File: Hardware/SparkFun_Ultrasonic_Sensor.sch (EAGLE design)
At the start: 67 parts, among them J4 Vertical Qwiic Connector, J6 Vertical Qwiic Connector, Q1 600mA/40V, U5 ULTRASONIC_SENSOR_TRANSMITTER, U6 LMV324, U7 STM8L051F3, U8 SP3232EB, U9 ULTRASONIC_SENSOR_RECEIVER

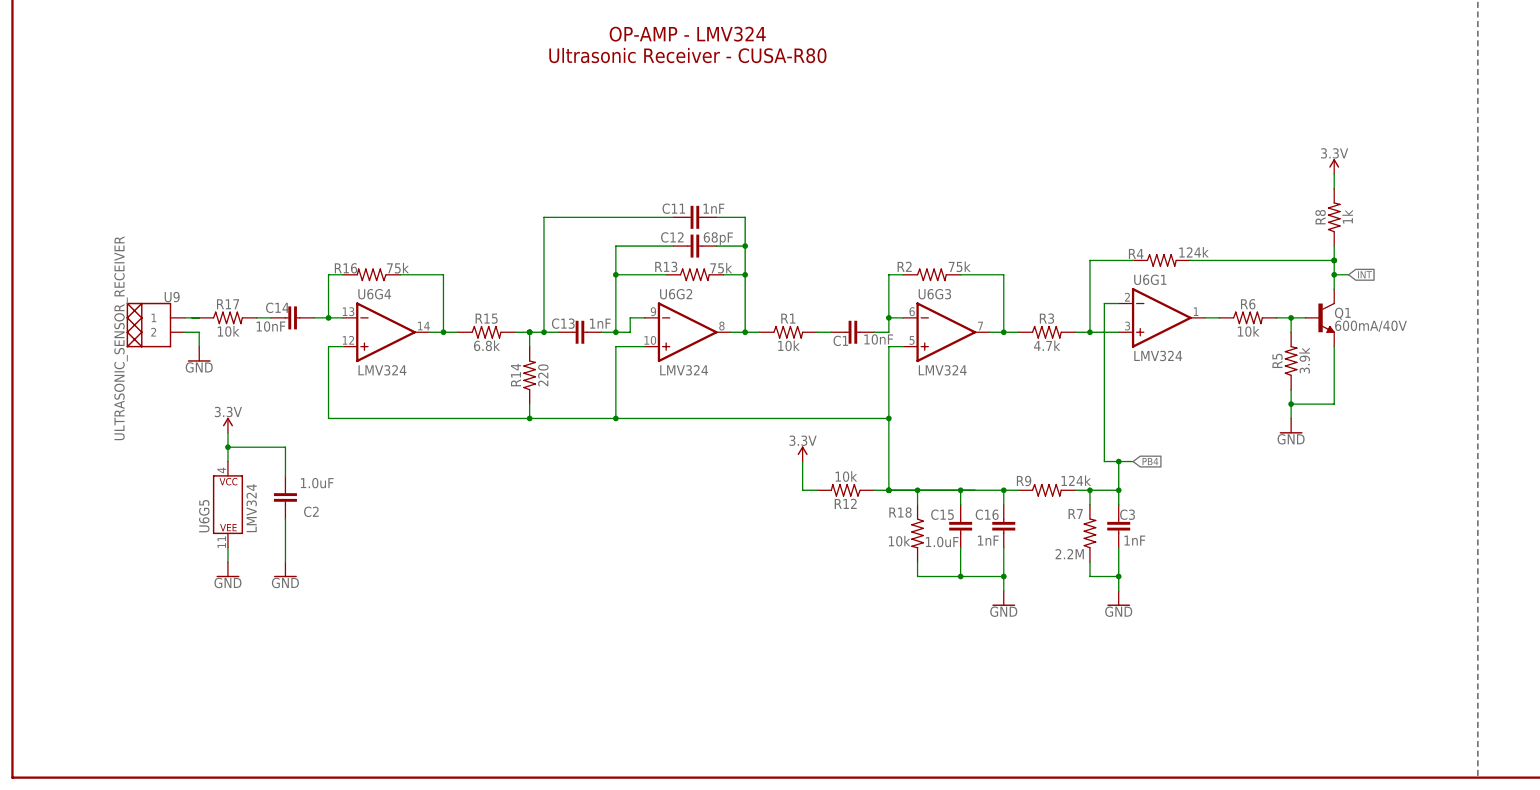
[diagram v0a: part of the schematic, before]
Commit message: Adds some notes on the op-amp stages
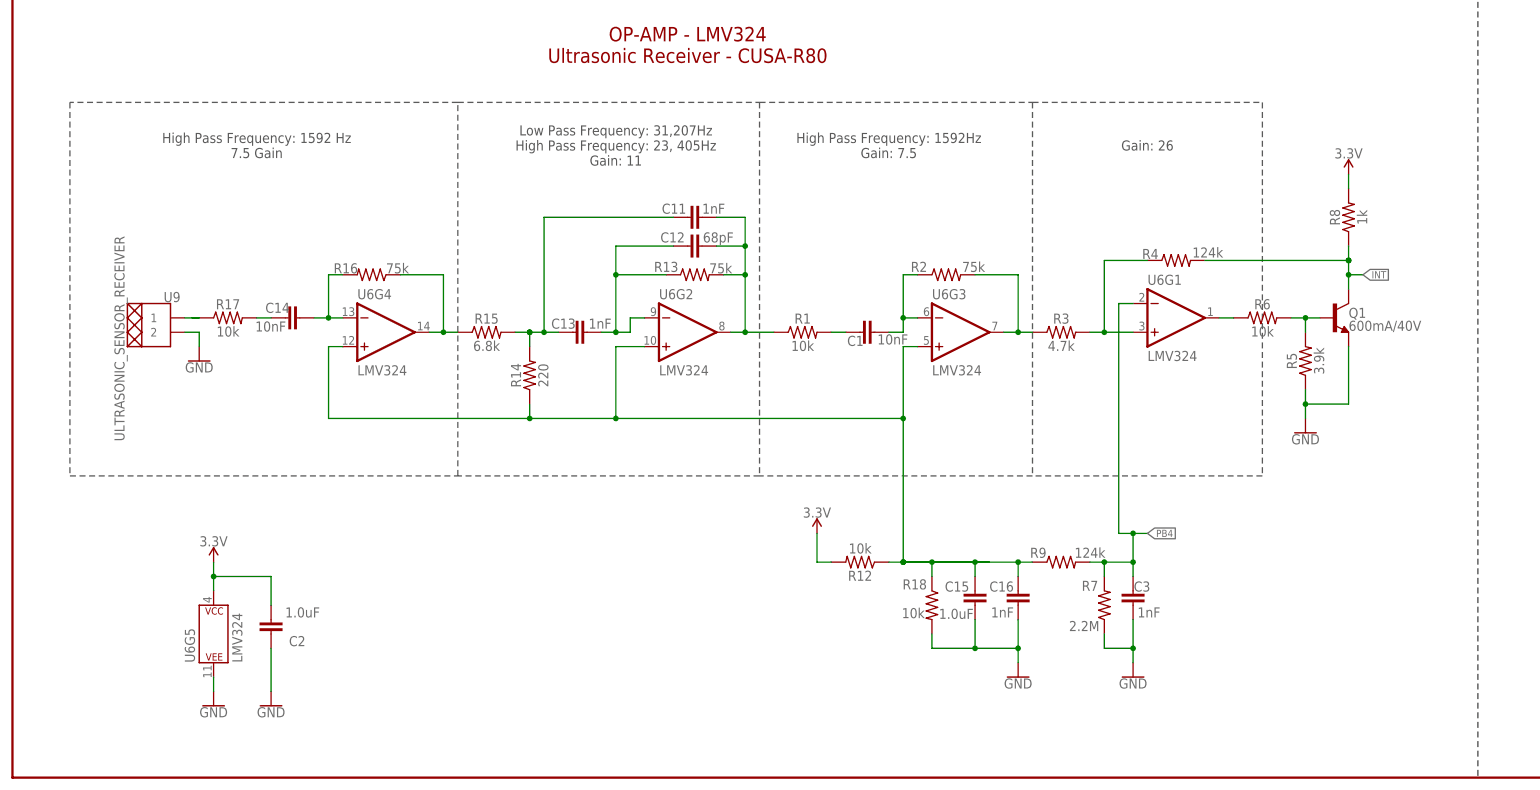
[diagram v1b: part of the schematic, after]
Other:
- note added: "Gain: 26"
- note added: "High Pass Frequency: 1592 Hz 7.5 Gain"
- note added: "High Pass Frequency: 1592Hz Gain: 7.5"
- note added: "Low Pass Frequency: 31,207Hz High Pass Frequency: 23, 405Hz Gain: 11"
- moved on the sheet: C1, C15, C16, C2, C3, Q1, R1, R12, R18, R2, R3, R4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
